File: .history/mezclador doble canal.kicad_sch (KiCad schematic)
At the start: 15 parts, among them J1 Conn_Coaxial, J2 Conn_Coaxial, J3 Conn_Coaxial, U1 NE5532

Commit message: completè el canal L
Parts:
- added JP1: Jumper_2_Open, personal:Jumper_Wire_10mm, symbol Jumper:Jumper_2_Open
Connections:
- net at C1.2: now also JP1.2 (B); no longer RV1.2
- new net: JP1.1 (A), RV1.2
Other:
- moved on the sheet: C1, C2
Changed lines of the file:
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@@
+	(wire
+		(pts
+			(xy 116.84 71.12) (xy 119.38 71.12)
+		)
+		(stroke
+			(width 0)
+			(type default)
+		)
+	)
 	(wire
 		(pts
@@
 	(wire
 		(pts
-			(xy 116.84 82.55) (xy 125.73 82.55)
+			(xy 116.84 82.55) (xy 132.08 82.55)
 		)
 		(stroke
@@
 	(wire
 		(pts
-			(xy 133.35 82.55) (xy 142.24 82.55)
+			(xy 139.7 82.55) (xy 142.24 82.55)
 		)
 		(stroke
@@
 	(wire
 		(pts
-			(xy 116.84 71.12) (xy 125.73 71.12)
-		)
-		(stroke
-			(width 0)
-			(type default)
-		)
-	)
-	(wire
-		(pts
 			(xy 86.36 86.36) (xy 86.36 90.17)
 		)
@@
 	(wire
 		(pts
-			(xy 133.35 71.12) (xy 142.24 71.12)
+			(xy 129.54 71.12) (xy 132.08 71.12)
+		)
+		(stroke
+			(width 0)
+			(type default)
+		)
+	)
+	(wire
+		(pts
+			(xy 139.7 71.12) (xy 142.24 71.12)
 		)
 		(stroke
@@
 	(symbol
 		(lib_id "Device:C_Polarized_US")
-		(at 129.54 71.12 270)
+		(at 135.89 71.12 270)
 		(unit 1)
 		(body_style 1)
@@
 		(fields_autoplaced yes)
 		(property "Reference" "C1"
-			(at 130.175 63.5 90)
+			(at 136.525 63.5 90)
 			(show_name no)
 			(do_not_autoplace no)
@@
 		)
 		(property "Value" "C_Polarized_US"
-			(at 130.175 66.04 90)
+			(at 136.525 66.04 90)
 			(show_name no)
 			(do_not_autoplace no)
@@
 		)
 		(property "Footprint" "Capacitor_THT:CP_Radial_D5.0mm_P2.50mm"
-			(at 129.54 71.12 0)
+			(at 135.89 71.12 0)
 			(hide yes)
 			(show_name no)
@@
 		)
 		(property "Datasheet" ""
-			(at 129.54 71.12 0)
+			(at 135.89 71.12 0)
 			(hide yes)
 			(show_name no)
@@
 		)
 		(property "Description" "Polarized capacitor, US symbol"
-			(at 129.54 71.12 0)
+			(at 135.89 71.12 0)
 			(hide yes)
 			(show_name no)
@@
 	)
 	(symbol
+		(lib_id "Jumper:Jumper_2_Open")
+		(at 124.46 71.12 0)
+		(unit 1)
+		(body_style 1)
+		(exclude_from_sim no)
+		(in_bom yes)
+		(on_board yes)
+		(in_pos_files yes)
+		(dnp no)
+		(fields_autoplaced yes)
+		(property "Reference" "JP1"
+			(at 124.46 64.77 0)
+			(show_name no)
+			(do_not_autoplace no)
+			(effects
+				(font
+					(size 1.27 1.27)
+				)
+			)
+		)
+		(property "Value" "Jumper_2_Open"
+			(at 124.46 67.31 0)
+			(show_name no)
+			(do_not_autoplace no)
+			(effects
+				(font
+					(size 1.27 1.27)
+				)
+			)
+		)
+		(property "Footprint" "personal:Jumper_Wire_10mm"
+			(at 124.46 71.12 0)
+			(hide yes)
+			(show_name no)
+			(do_not_autoplace no)
+			(effects
+				(font
+					(size 1.27 1.27)
+				)
+			)
+		)
+		(property "Datasheet" ""
+			(at 124.46 71.12 0)
+			(hide yes)
+			(show_name no)
+			(do_not_autoplace no)
+			(effects
+				(font
+					(size 1.27 1.27)
+				)
+			)
+		)
+		(property "Description" "Jumper, 2-pole, open"
+			(at 124.46 71.12 0)
+			(hide yes)
+			(show_name no)
+			(do_not_autoplace no)
+			(effects
+				(font
+					(size 1.27 1.27)
+				)
+			)
+		)
+		(pin "1"
+		)
+		(pin "2"
+		)
+		(instances
+			(project "mezclador doble canal"
+				(path "/1fd6db7d-bb33-43be-9c70-fde303eb7f84"
+					(reference "JP1")
+					(unit 1)
+				)
+			)
+		)
+	)
+	(symbol
 		(lib_id "power:GND")
 		(at 86.36 101.6 0)
@@
 	(symbol
 		(lib_id "Device:C_Polarized_US")
-		(at 129.54 82.55 270)
+		(at 135.89 82.55 270)
 		(unit 1)
 		(body_style 1)
@@
 		(fields_autoplaced yes)
 		(property "Reference" "C2"
-			(at 130.175 74.93 90)
+			(at 136.525 74.93 90)
 			(show_name no)
 			(do_not_autoplace no)
@@
 		)
 		(property "Value" "C_Polarized_US"
-			(at 130.175 77.47 90)
+			(at 136.525 77.47 90)
 			(show_name no)
 			(do_not_autoplace no)
@@
 		)
 		(property "Footprint" "Capacitor_THT:CP_Radial_D5.0mm_P2.50mm"
-			(at 129.54 82.55 0)
+			(at 135.89 82.55 0)
 			(hide yes)
 			(show_name no)
@@
 		)
 		(property "Datasheet" ""
-			(at 129.54 82.55 0)
+			(at 135.89 82.55 0)
 			(hide yes)
 			(show_name no)
@@
 		)
 		(property "Description" "Polarized capacitor, US symbol"
-			(at 129.54 82.55 0)
-			(hide yes)
-			(show_name no)
+			(at 135.89 82.55 0)
+			(hide yes)
+			(show_name no)

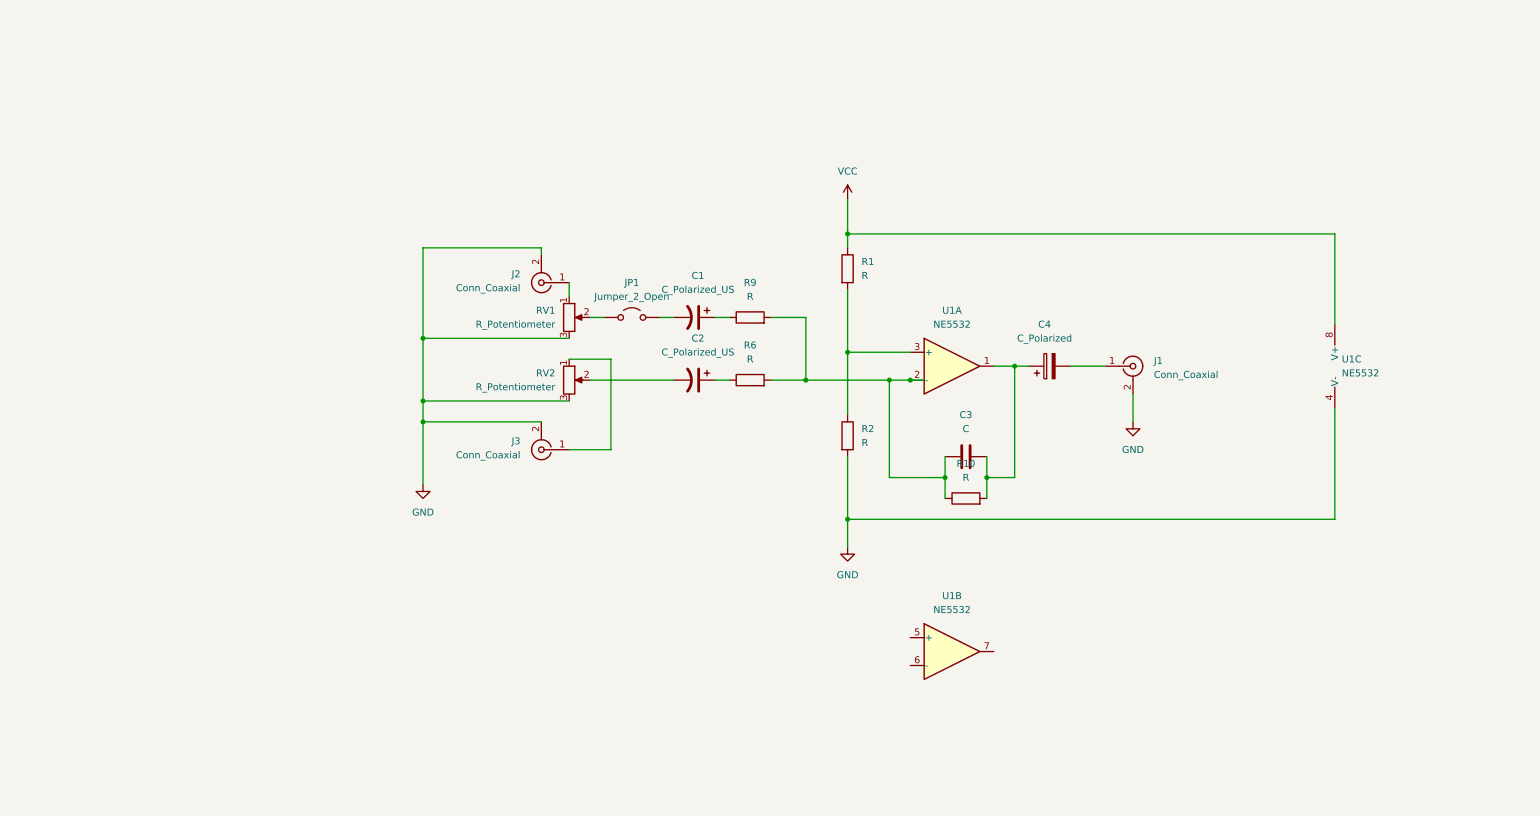
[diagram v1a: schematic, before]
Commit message: agregando canal r
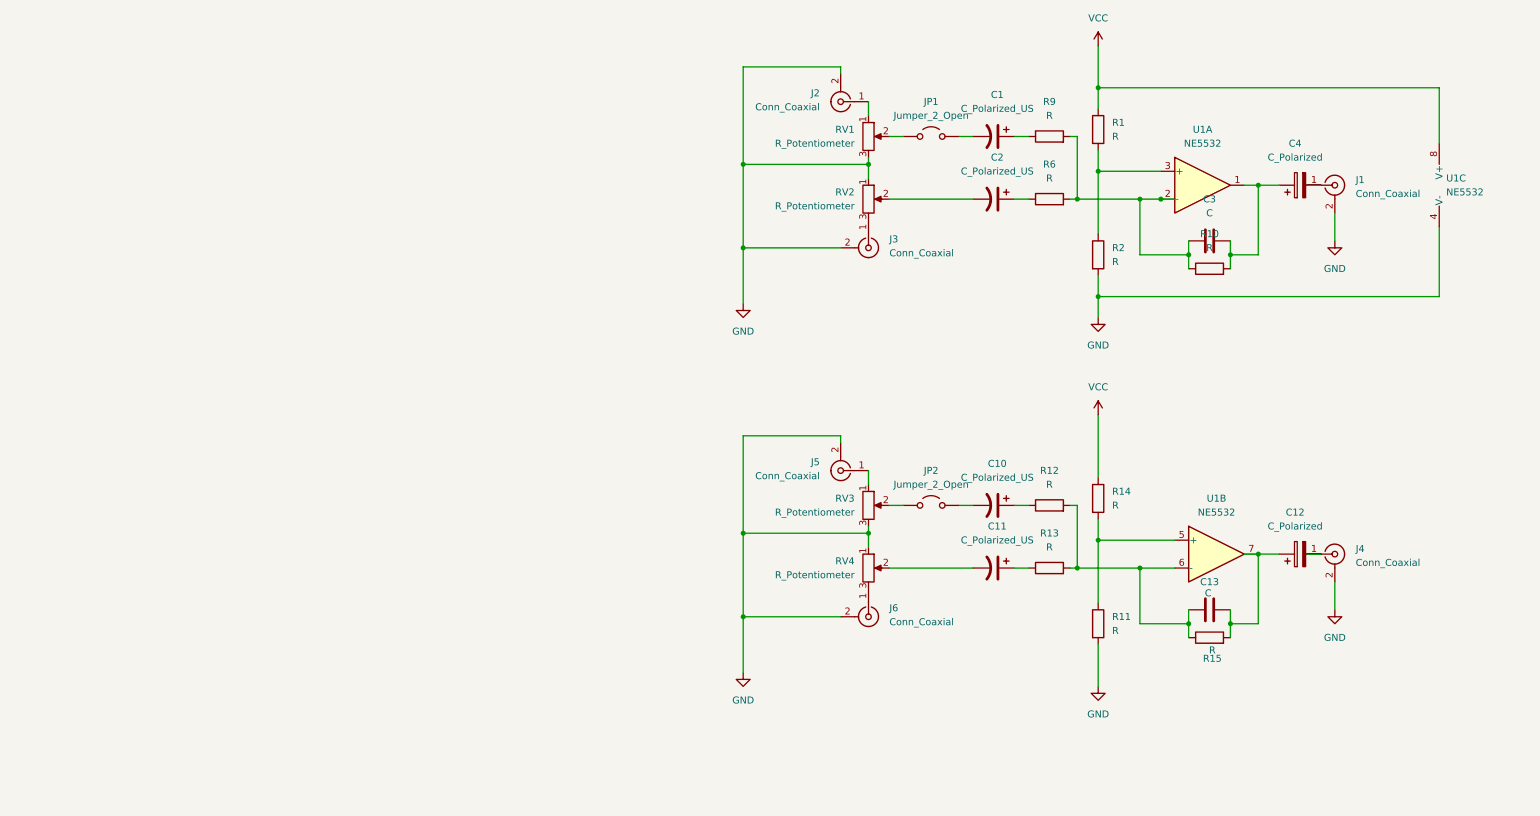
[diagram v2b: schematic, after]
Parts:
- added C10, C11: C_Polarized_US, Capacitor_THT:CP_Radial_D5.0mm_P2.50mm, symbol Device:C_Polarized_US
- added C12: C_Polarized, Capacitor_THT:CP_Radial_D5.0mm_P2.50mm, symbol Device:C_Polarized
- added C13: C, Capacitor_THT:C_Disc_D5.0mm_W2.5mm_P5.00mm, symbol Device:C
- added J4, J5, J6: Conn_Coaxial, Connector:JWT_A3963_1x02_P3.96mm_Vertical, symbol Connector:Conn_Coaxial
- added JP2: Jumper_2_Open, personal:Jumper_Wire_10mm, symbol Jumper:Jumper_2_Open
- added R11, R12, R13, R14, R15: R, Resistor_THT:R_Axial_DIN0207_L6.3mm_D2.5mm_P10.16mm_Horizontal, symbol Device:R
- added RV3, RV4: R_Potentiometer, Potentiometer_THT:Potentiometer_Bourns_3296W_Vertical, symbol Device:R_Potentiometer
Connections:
- net GND: now also RV2.1, J4.2 (Ext), J5.2 (Ext), J6.2 (Ext), R11.2, RV3.3, RV4.1; no longer RV2.3
- net VCC: now also R14.1
- net at U1.5 (+): now also R11.1, R14.2
- net at U1.6 (-): now also C13.1, R12.2, R13.2, R15.1
- net at U1.7: now also C12.1, C13.2, R15.2
- net at J3.1 (In): now also RV2.3; no longer RV2.1
- new net: C11.2, RV4.2
- new net: J6.1 (In), RV4.3
- new net: C10.1, R12.1
- new net: C11.1, R13.1
- new net: C12.2, J4.1 (In)
- new net: J5.1 (In), RV3.1
- new net: JP2.1 (A), RV3.2
- new net: C10.2, JP2.2 (B)
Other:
- moved on the sheet: C1, C2, C3, C4, J1, J2, J3, JP1, R1, R10, R2, R6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

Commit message: trabajando canal R
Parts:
- removed JP2: Jumper_2_Open, personal:Jumper_Wire_10mm, symbol Jumper:Jumper_2_Open
- added J7: Screw_Terminal_01x02, Connector:JWT_A3963_1x02_P3.96mm_Vertical, symbol Connector:Screw_Terminal_01x02
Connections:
- net GND: now also J7.2 (Pin_2)
- net VCC: now also J7.1 (Pin_1)
- net at RV3.2: now also C10.2
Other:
- moved on the sheet: C1, C10, C11, C12, C13, C2, C3, C4, J1, J2, J3, J4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

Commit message: agregando pads potenciometros
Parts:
- RV2, RV3: footprint Potentiometer_THT:Potentiometer_Bourns_3296W_Vertical -> personal:potentiometer pads
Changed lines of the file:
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@@
 			)
 		)
-		(property "Footprint" "Potentiometer_THT:Potentiometer_Bourns_3296W_Vertical"
+		(property "Footprint" "personal:potentiometer pads"
 			(at 142.24 52.07 0)
 			(hide yes)
@@
 			)
 		)
-		(property "Footprint" "Potentiometer_THT:Potentiometer_Bourns_3296W_Vertical"
+		(property "Footprint" "personal:potentiometer pads"
 			(at 142.24 90.17 0)
 			(hide yes)

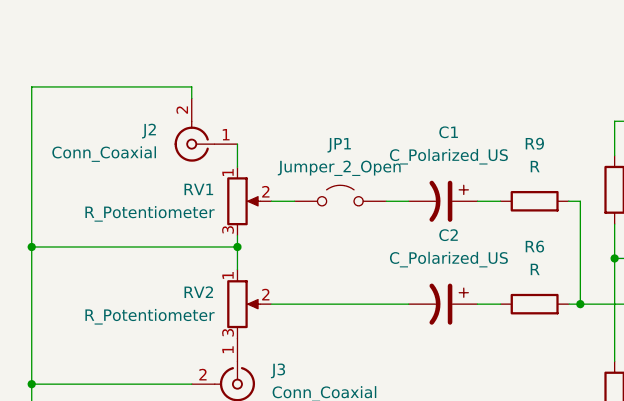
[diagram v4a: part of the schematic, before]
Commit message: mejorando distribucion de componentes
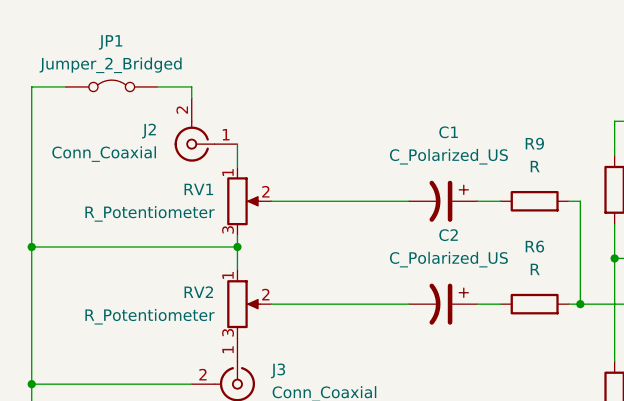
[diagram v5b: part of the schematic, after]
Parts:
- removed JP1: Jumper_2_Open, personal:Jumper_Wire_10mm, symbol Jumper:Jumper_2_Open
- added JP1: Jumper_2_Bridged, personal:Jumper_Wire_10mm, symbol Jumper:Jumper_2_Bridged
- J1, J2, J3, J5, J7: footprint Connector:JWT_A3963_1x02_P3.96mm_Vertical -> personal:double wire
- RV1: footprint Potentiometer_THT:Potentiometer_Bourns_3296W_Vertical -> personal:potentiometer pads
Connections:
- net GND: now also JP1.1 (A); no longer J2.2 (Ext)
- net at C1.2: now also RV1.2
- new net: J2.2 (Ext), JP1.2 (B)
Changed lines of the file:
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@@
 	(wire
 		(pts
-			(xy 146.05 40.64) (xy 148.59 40.64)
+			(xy 146.05 40.64) (xy 161.29 40.64)
 		)
 		(stroke
@@
 	(wire
 		(pts
-			(xy 137.16 27.94) (xy 119.38 27.94)
+			(xy 224.79 99.06) (xy 222.25 99.06)
 		)
 		(stroke
@@
 	(wire
 		(pts
-			(xy 224.79 99.06) (xy 222.25 99.06)
+			(xy 119.38 27.94) (xy 123.19 27.94)
 		)
 		(stroke
@@
 	(wire
 		(pts
+			(xy 133.35 27.94) (xy 137.16 27.94)
+		)
+		(stroke
+			(width 0)
+			(type default)
+		)
+	)
+	(wire
+		(pts
 			(xy 227.33 69.85) (xy 246.38 69.85)
 		)
@@
 	(wire
 		(pts
-			(xy 158.75 40.64) (xy 161.29 40.64)
-		)
-		(stroke
-			(width 0)
-			(type default)
-		)
-	)
-	(wire
-		(pts
 			(xy 168.91 40.64) (xy 171.45 40.64)
 		)
@@
 	)
 	(symbol
-		(lib_id "Jumper:Jumper_2_Open")
-		(at 153.67 40.64 0)
-		(unit 1)
-		(body_style 1)
-		(exclude_from_sim no)
-		(in_bom yes)
-		(on_board yes)
-		(in_pos_files yes)
-		(dnp no)
-		(fields_autoplaced yes)
-		(property "Reference" "JP1"
-			(at 153.67 34.29 0)
-			(show_name no)
-			(do_not_autoplace no)
-			(effects
-				(font
-					(size 1.27 1.27)
-				)
-			)
-		)
-		(property "Value" "Jumper_2_Open"
-			(at 153.67 36.83 0)
-			(show_name no)
-			(do_not_autoplace no)
-			(effects
-				(font
-					(size 1.27 1.27)
-				)
-			)
-		)
-		(property "Footprint" "personal:Jumper_Wire_10mm"
-			(at 153.67 40.64 0)
-			(hide yes)
-			(show_name no)
-			(do_not_autoplace no)
-			(effects
-				(font
-					(size 1.27 1.27)
-				)
-			)
-		)
-		(property "Datasheet" ""
-			(at 153.67 40.64 0)
-			(hide yes)
-			(show_name no)
-			(do_not_autoplace no)
-			(effects
-				(font
-					(size 1.27 1.27)
-				)
-			)
-		)
-		(property "Description" "Jumper, 2-pole, open"
-			(at 153.67 40.64 0)
-			(hide yes)
-			(show_name no)
-			(do_not_autoplace no)
-			(effects
-				(font
-					(size 1.27 1.27)
-				)
-			)
-		)
-		(pin "1"
-		)
-		(pin "2"
-		)
-		(instances
-			(project "mezclador doble canal"
-				(path "/1fd6db7d-bb33-43be-9c70-fde303eb7f84"
-					(reference "JP1")
-					(unit 1)
-				)
-			)
-		)
-	)
-	(symbol
 		(lib_id "Connector:Conn_Coaxial")
 		(at 142.24 60.96 270)
@@
 			)
 		)
-		(property "Footprint" "Connector:JWT_A3963_1x02_P3.96mm_Vertical"
+		(property "Footprint" "personal:double wire"
 			(at 142.24 60.96 0)
 			(hide yes)
@@
 			)
 		)
-		(property "Footprint" "Potentiometer_THT:Potentiometer_Bourns_3296W_Vertical"
+		(property "Footprint" "personal:potentiometer pads"
 			(at 142.24 40.64 0)
 			(hide yes)
@@
 			)
 		)
-		(property "Footprint" "Connector:JWT_A3963_1x02_P3.96mm_Vertical"
+		(property "Footprint" "personal:double wire"
 			(at 260.35 48.26 0)
 			(hide yes)
@@
 			)
 		)
-		(property "Footprint" "Connector:JWT_A3963_1x02_P3.96mm_Vertical"
+		(property "Footprint" "personal:double wire"
 			(at 137.16 83.82 0)
 			(hide yes)
@@
 	)
 	(symbol
+		(lib_id "Jumper:Jumper_2_Bridged")
+		(at 128.27 27.94 0)
+		(unit 1)
+		(body_style 1)
+		(exclude_from_sim no)
+		(in_bom yes)
+		(on_board yes)
+		(in_pos_files yes)
+		(dnp no)
+		(fields_autoplaced yes)
+		(property "Reference" "JP1"
+			(at 128.27 22.86 0)
+			(show_name no)
+			(do_not_autoplace no)
+			(effects
+				(font
+					(size 1.27 1.27)
+				)
+			)
+		)
+		(property "Value" "Jumper_2_Bridged"
+			(at 128.27 25.4 0)
+			(show_name no)
+			(do_not_autoplace no)
+			(effects
+				(font
+					(size 1.27 1.27)
+				)
+			)
+		)
+		(property "Footprint" "personal:Jumper_Wire_10mm"
+			(at 128.27 27.94 0)
+			(hide yes)
+			(show_name no)
+			(do_not_autoplace no)
+			(effects
+				(font
+					(size 1.27 1.27)
+				)
+			)
+		)
+		(property "Datasheet" ""
+			(at 128.27 33.02 0)
+			(hide yes)
+			(show_name no)
+			(do_not_autoplace no)
+			(effects
+				(font
+					(size 1.27 1.27)
+				)
+			)
+		)
+		(property "Description" "Jumper, 2-pole, closed/bridged"
+			(at 128.27 35.56 0)
+			(hide yes)
+			(show_name no)
+			(do_not_autoplace no)
+			(effects
+				(font
+					(size 1.27 1.27)
+				)
+			)
+		)
+		(pin "2"
+		)
+		(pin "1"
+		)
+		(instances
+			(project "mezclador doble canal"
+				(path "/1fd6db7d-bb33-43be-9c70-fde303eb7f84"
+					(reference "JP1")
+					(unit 1)
+				)
+			)
+		)
+	)
+	(symbol
 		(lib_id "Connector:Conn_Coaxial")
 		(at 227.33 49.53 0)
@@
 			)
 		)
-		(property "Footprint" "Connector:JWT_A3963_1x02_P3.96mm_Vertical"
+		(property "Footprint" "personal:double wire"
 			(at 227.33 49.53 0)
 			(hide yes)
@@
 			)
 		)
-		(property "Footprint" "Connector:JWT_A3963_1x02_P3.96mm_Vertical"
+		(property "Footprint" "personal:double wire"
 			(at 137.16 34.29 0)
 			(hide yes)
